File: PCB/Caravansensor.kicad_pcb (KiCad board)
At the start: 2 copper layers, 186 parts, among them J1 Conn_01x06, J5 DB25_Female, Q1 MMBTA92, Q10 BSS138, Q11 BSS138, Q12 BSS138, Q13 BSS83P, Q14 BSS83P, Q15 BSS83P, Q16 BSS83P, Q17 BSS138, Q18 BSS138, Q19 BSS138, Q2 MMBTA92, Q20 BSS138, Q21 BSS138, Q22 BSS138, Q23 BSS138, Q24 BSS138, Q25 BSS83P, Q26 BSS83P, Q27 BSS83P, Q28 BSS83P, Q3 BC856, Q4 BC846, Q5 BSS138, Q6 BSS138, Q7 BSS138, Q8 BSS138, Q9 BSS138, U1 MPX53, U2 MPX53, U3 HX711, U4 HX711, U5 ESP32-WROOM-32D, U6 LMV321, U7 LMV321

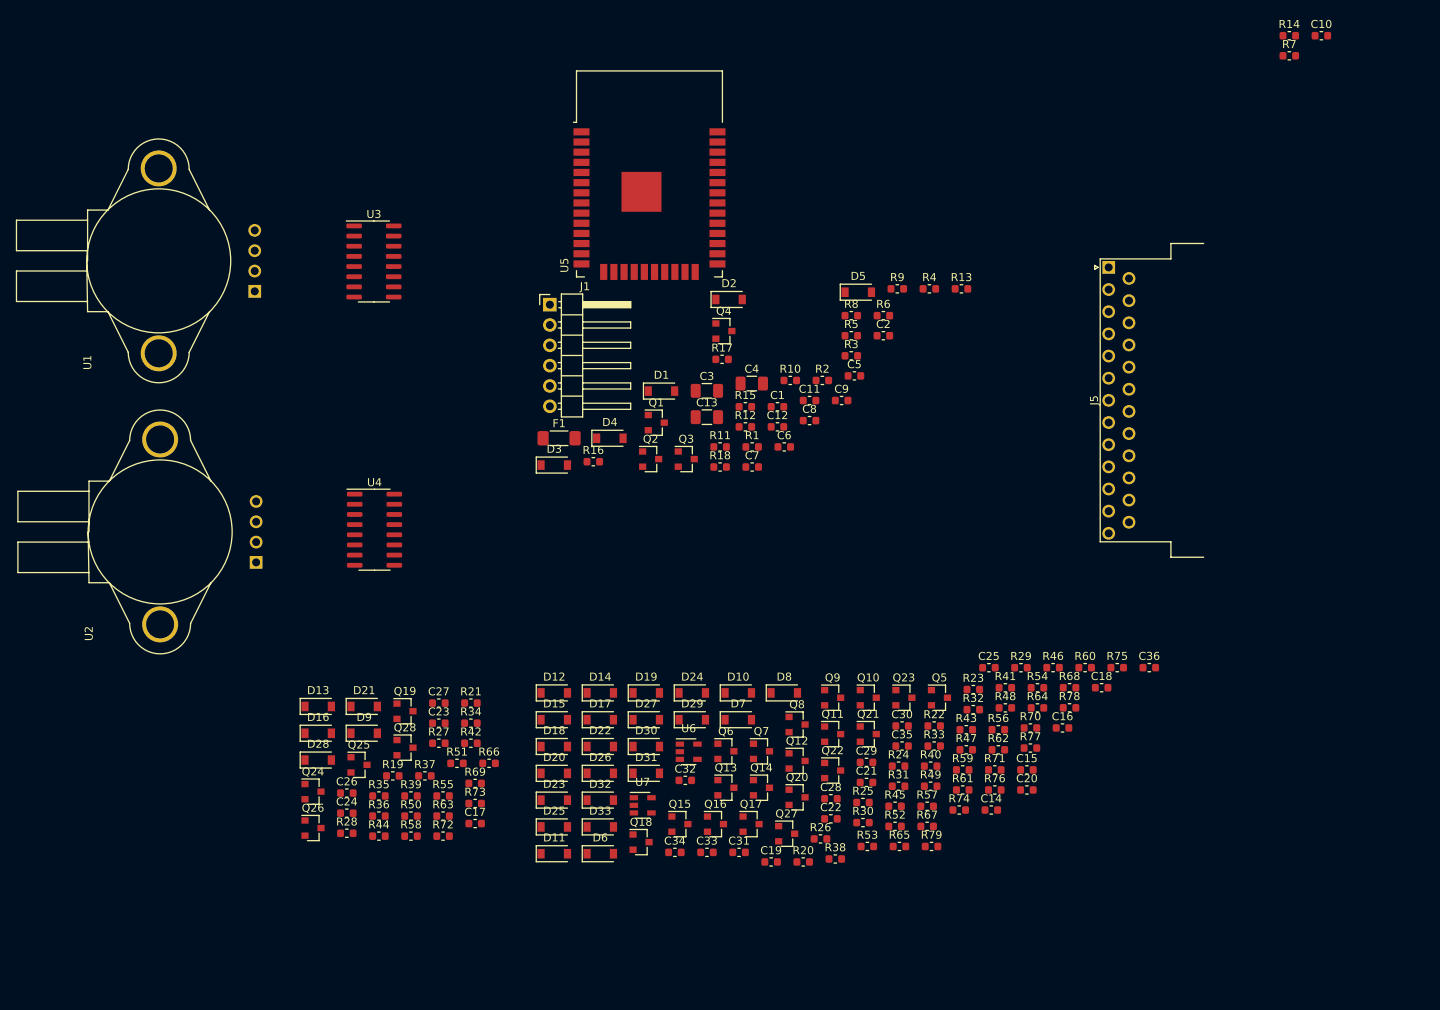
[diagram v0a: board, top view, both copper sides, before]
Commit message: Layout complete, LIN, Added, 1wire added, Power supply added
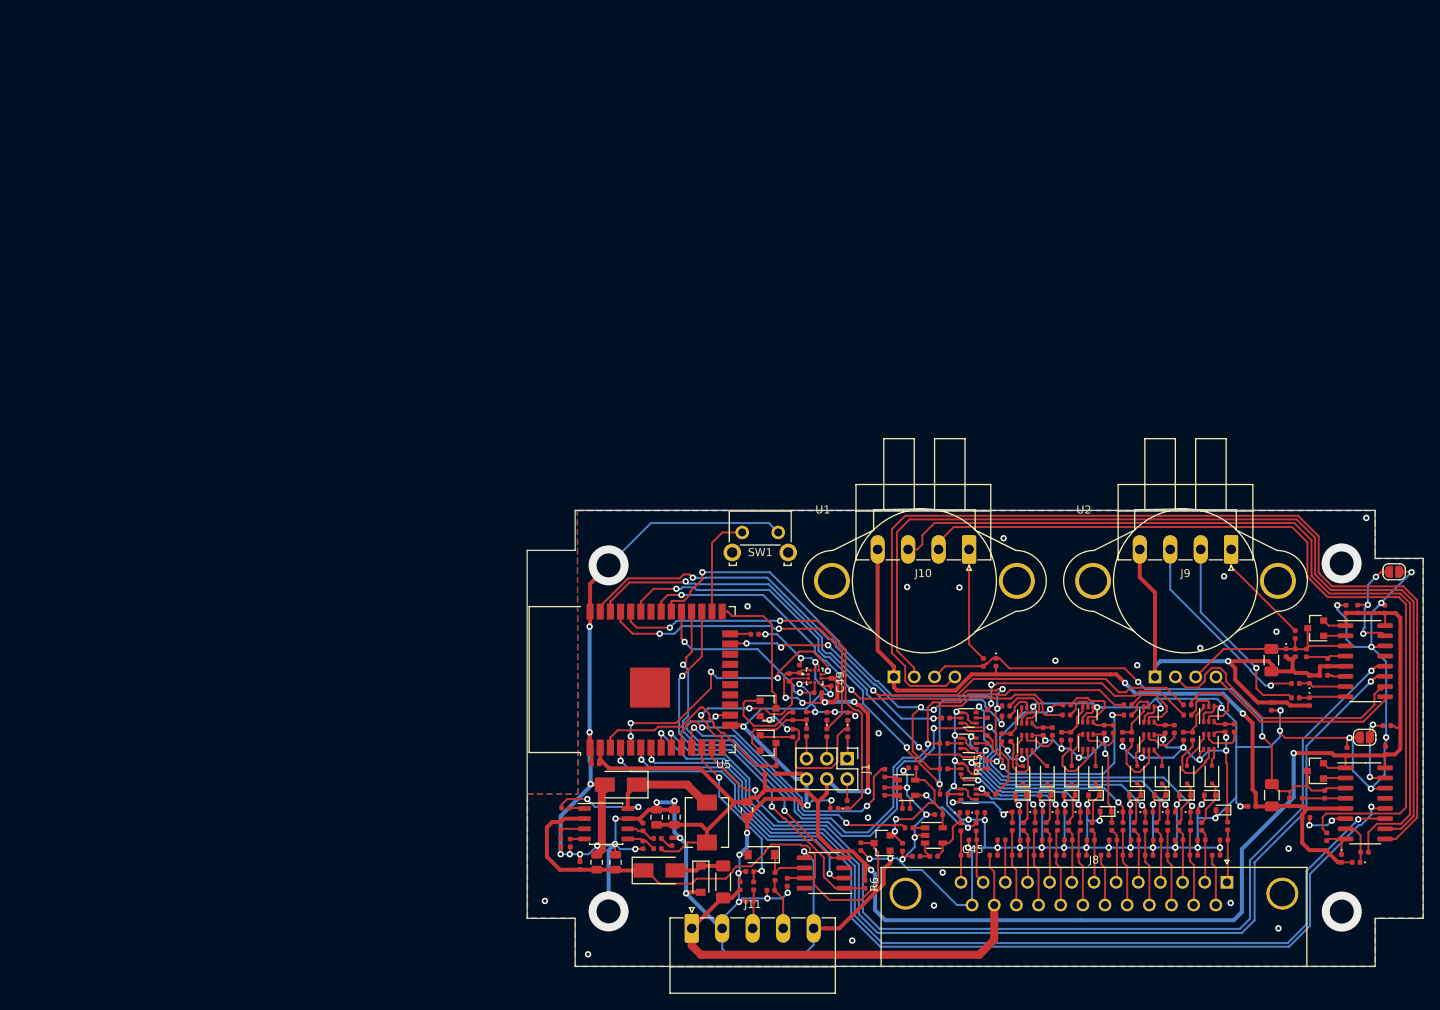
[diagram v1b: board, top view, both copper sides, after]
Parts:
- removed the C27 at (89.9, 123.1)
- removed the C34 at (119.4, 141.8)
- removed the D4 at (111.3, 90.0)
- removed the D5 at (142.4, 71.7)
- removed J5: DB25_Female, Connector_Dsub:DSUB-25_Female_Horizontal_P2.77x2.54mm_EdgePinOffset9.40mm
- removed Q17, Q18, Q19, Q20, Q21, Q22, Q23, Q24: BSS138, Package_TO_SOT_SMD:SOT-23
- removed Q25, Q26, Q27, Q28: BSS83P, Package_TO_SOT_SMD:SOT-23
- removed the R16 at (109.2, 92.9)
- removed the R8 at (141.5, 74.7)
- added C14: 100n, Capacitor_SMD:C_0402_1005Metric, F.Cu at (133.5, 145.5)
- added C15: 100p, Capacitor_SMD:C_0402_1005Metric, F.Cu at (131.4, 146.5)
- added C16: 4u7, Capacitor_SMD:C_0805_2012Metric, F.Cu at (112.0, 143.0)
- added C17: 4u7, Capacitor_SMD:C_0805_2012Metric, F.Cu at (109.7, 143.0)
- added C18: 1n, Capacitor_SMD:C_0402_1005Metric, F.Cu at (117.3, 140.0)
- added C19: 47p, Capacitor_SMD:C_0402_1005Metric, F.Cu at (115.4, 138.6)
- added C20: 100n, Capacitor_SMD:C_0402_1005Metric, F.Cu at (106.4, 140.6)
- added C21: 100n, Capacitor_SMD:C_0402_1005Metric, F.Cu at (105.8, 136.2)
- added C22: 47u, Capacitor_SMD:C_0805_2012Metric, F.Cu at (117.2, 137.4)
- added C23: 47u, Capacitor_SMD:C_0805_2012Metric, F.Cu at (119.4, 137.4)
- added C37: 10n, Capacitor_SMD:C_0402_1005Metric, F.Cu at (165.8, 140.2)
- added C44: 100n, Capacitor_SMD:C_0402_1005Metric, F.Cu at (159.3, 142.1)
- added C47: 100n, Capacitor_SMD:C_0402_1005Metric, F.Cu at (142.7, 141.0)
- added C48: 100n, Capacitor_SMD:C_0402_1005Metric, F.Cu at (147.9, 141.1)
- added C49: 100n, Capacitor_SMD:C_0402_1005Metric, F.Cu at (138.9, 120.5)
- added C50: 47u, Capacitor_SMD:C_0805_2012Metric, F.Cu at (128.5, 136.4)
- added C51: 1n, Capacitor_SMD:C_0402_1005Metric, F.Cu at (132.1, 131.4)
- added C52: 100p, Capacitor_SMD:C_0402_1005Metric, F.Cu at (128.8, 147.8)
- added C53: 100n, Capacitor_SMD:C_0402_1005Metric, F.Cu at (135.0, 118.8)
- added D3: SMF16A, Diode_SMD:D_SOD-123, F.Cu at (130.2, 142.0)
- added D34: RCLAMP0521P-N, Diode_SMD:D_0402_1005Metric, F.Cu at (195.8, 116.8)
- added D35: RCLAMP0521P-N, Diode_SMD:D_0402_1005Metric, F.Cu at (202.8, 142.5)
- added D36: RCLAMP0521P-N, Diode_SMD:D_0402_1005Metric, F.Cu at (198.8, 122.9)
- added D37: RCLAMP0521P-N, Diode_SMD:D_0402_1005Metric, F.Cu at (204.6, 143.0)
- added D38: RCLAMP0521P-N, Diode_SMD:D_0402_1005Metric, F.Cu at (198.8, 120.1)
- added D39: RCLAMP0521P-N, Diode_SMD:D_0402_1005Metric, F.Cu at (128.8, 144.1)
- added D40: RCLAMP0521P-N, Diode_SMD:D_0402_1005Metric, F.Cu at (141.0, 124.8)
- added D41: RCLAMP0521P-N, Diode_SMD:D_0402_1005Metric, F.Cu at (138.4, 124.7)
- added D42: RCLAMP0521P-N, Diode_SMD:D_0402_1005Metric, F.Cu at (135.9, 124.7)
- added D43: RCLAMP0521P-N, Diode_SMD:D_0402_1005Metric, F.Cu at (139.3, 136.3)
- added D6: RCLAMP0521P-N, Diode_SMD:D_0402_1005Metric, F.Cu at (178.7, 136.7)
- added J10: Conn_01x04, Connector_Phoenix_MC:PhoenixContact_MC_1,5_4-G-3.81_1x04_P3.81mm_Horizontal, F.Cu at (156.2, 103.9)
- added J11: Conn_01x05, Connector_Phoenix_MC:PhoenixContact_MC_1,5_5-G-3.81_1x05_P3.81mm_Horizontal, F.Cu at (121.5, 151.3)
- added J8: DB25_Female, Connector_Dsub:DSUB-25_Female_Horizontal_P2.77x2.84mm_EdgePinOffset7.70mm_Housed_MountingHolesOffset9.12mm, F.Cu at (188.4, 145.5)
- added J9: Conn_01x04, Connector_Phoenix_MC:PhoenixContact_MC_1,5_4-G-3.81_1x04_P3.81mm_Horizontal, F.Cu at (189.0, 103.9)
- added JP2: Jumper_2_Open, Jumper:SolderJumper-2_P1.3mm_Open_RoundedPad1.0x1.5mm, F.Cu at (205.7, 127.4)
- added JP3: Jumper_2_Open, Jumper:SolderJumper-2_P1.3mm_Open_RoundedPad1.0x1.5mm, F.Cu at (209.3, 106.7)
- added L1: SLO0630H6R8MTT, Inductor_SMD:L_Neosid_SM-PIC0512H, F.Cu at (123.4, 138.0)
- added L2: L, Inductor_SMD:L_0402_1005Metric, F.Cu at (191.6, 136.0)
- added L3: L, Inductor_SMD:L_0402_1005Metric, F.Cu at (194.0, 123.5)
- added R12: 29k4, Resistor_SMD:R_0402_1005Metric, F.Cu at (119.1, 140.4)
- added R7: 100r, Resistor_SMD:R_0402_1005Metric, F.Cu at (132.0, 144.8)
- added R80: 100r, Resistor_SMD:R_0402_1005Metric, F.Cu at (158.0, 118.0)
- added R81: 100r, Resistor_SMD:R_0402_1005Metric, F.Cu at (200.9, 139.8)
- added R82: 100r, Resistor_SMD:R_0402_1005Metric, F.Cu at (205.6, 141.7)
- added R83: 100r, Resistor_SMD:R_0402_1005Metric, F.Cu at (197.0, 114.5)
- added R84: 100r, Resistor_SMD:R_0402_1005Metric, F.Cu at (197.0, 122.4)
- added R85: 100r, Resistor_SMD:R_0402_1005Metric, F.Cu at (197.0, 120.7)
- added R86: 4k7, Resistor_SMD:R_0402_1005Metric, F.Cu at (133.7, 119.9)
- added R87: 4k7, Resistor_SMD:R_0402_1005Metric, F.Cu at (137.3, 121.8)
- added R88: 12k, Resistor_SMD:R_0402_1005Metric, F.Cu at (130.7, 131.4)
- added R89: 100r, Resistor_SMD:R_0402_1005Metric, F.Cu at (129.3, 145.9)
- added R90: 10k, Resistor_SMD:R_0402_1005Metric, F.Cu at (208.4, 125.9)
- added R91: 10k, Resistor_SMD:R_0402_1005Metric, F.Cu at (204.8, 111.3)
- added SW1: TS-1093A-A12B3-D2, Button_Switch_THT:SW_Tactile_SKHH_Angled, F.Cu at (127.9, 101.8)
- added U10: BMP388, Caravansensor:PQFN50P200X200X80-10N, F.Cu at (136.9, 119.8)
- added U11: ME6209A50M3G, Package_TO_SOT_SMD:SOT-23, F.Cu at (145.3, 140.6)
- added U6: TJA1021T, Package_SO:SOIC-8_3.9x4.9mm_P1.27mm, F.Cu at (138.1, 144.3)
- added U7: TPS54331D, Package_SO:SOIC-8_3.9x4.9mm_P1.27mm, F.Cu at (110.8, 138.2)
- C1, C10, C11, C12, C2, C5, C6, C7, C8, C9: footprint Capacitor_SMD:C_0603_1608Metric -> Capacitor_SMD:C_0402_1005Metric
- C13: value 10u -> 100n; footprint Capacitor_SMD:C_1206_3216Metric -> Capacitor_SMD:C_0402_1005Metric
- C24: renamed from C14; footprint Capacitor_SMD:C_0603_1608Metric -> Capacitor_SMD:C_0402_1005Metric
- C25: renamed from C15; footprint Capacitor_SMD:C_0603_1608Metric -> Capacitor_SMD:C_0402_1005Metric
- C26: renamed from C16; footprint Capacitor_SMD:C_0603_1608Metric -> Capacitor_SMD:C_0402_1005Metric
- C27: renamed from C17; footprint Capacitor_SMD:C_0603_1608Metric -> Capacitor_SMD:C_0402_1005Metric
- C28: renamed from C18; footprint Capacitor_SMD:C_0603_1608Metric -> Capacitor_SMD:C_0402_1005Metric
- C29: renamed from C19; footprint Capacitor_SMD:C_0603_1608Metric -> Capacitor_SMD:C_0402_1005Metric
- C30: renamed from C20; footprint Capacitor_SMD:C_0603_1608Metric -> Capacitor_SMD:C_0402_1005Metric
- C31: renamed from C21; footprint Capacitor_SMD:C_0603_1608Metric -> Capacitor_SMD:C_0402_1005Metric
- C32: renamed from C22; footprint Capacitor_SMD:C_0603_1608Metric -> Capacitor_SMD:C_0402_1005Metric
- C33: renamed from C23; footprint Capacitor_SMD:C_0603_1608Metric -> Capacitor_SMD:C_0402_1005Metric
- C34: renamed from C24; footprint Capacitor_SMD:C_0603_1608Metric -> Capacitor_SMD:C_0402_1005Metric
- C35: renamed from C25; footprint Capacitor_SMD:C_0603_1608Metric -> Capacitor_SMD:C_0402_1005Metric
- C36: renamed from C26; footprint Capacitor_SMD:C_0603_1608Metric -> Capacitor_SMD:C_0402_1005Metric
- C38: renamed from C28; footprint Capacitor_SMD:C_0603_1608Metric -> Capacitor_SMD:C_0402_1005Metric
- C39: renamed from C29; footprint Capacitor_SMD:C_0603_1608Metric -> Capacitor_SMD:C_0402_1005Metric
- C40: renamed from C30; footprint Capacitor_SMD:C_0603_1608Metric -> Capacitor_SMD:C_0402_1005Metric
- C41: renamed from C31; footprint Capacitor_SMD:C_0603_1608Metric -> Capacitor_SMD:C_0402_1005Metric
- C42: renamed from C32; footprint Capacitor_SMD:C_0603_1608Metric -> Capacitor_SMD:C_0402_1005Metric
- C43: renamed from C33; footprint Capacitor_SMD:C_0603_1608Metric -> Capacitor_SMD:C_0402_1005Metric
- C45: renamed from C35; footprint Capacitor_SMD:C_0603_1608Metric -> Capacitor_SMD:C_0402_1005Metric
- C46: renamed from C36; footprint Capacitor_SMD:C_0603_1608Metric -> Capacitor_SMD:C_0402_1005Metric
- D10, D11, D12, D22, D23, D24: value D -> 1N4148WS; footprint Diode_SMD:D_SOD-123 -> Diode_SMD:D_SOD-323F
- D13, D25: value D -> ESD5Z15V; footprint Diode_SMD:D_SOD-123 -> Diode_SMD:D_SOD-523
- D14, D15, D16, D26, D27, D28, D29, D30: value SMF16A -> ESD5Z15V; footprint Diode_SMD:D_SOD-123 -> Diode_SMD:D_SOD-523
- D17, D18, D19, D20, D31, D32, D33, D7, D8: value SMF16A -> RCLAMP0521P-N; footprint Diode_SMD:D_SOD-123 -> Diode_SMD:D_0402_1005Metric
- D2: value D -> B340A; footprint Diode_SMD:D_SOD-123 -> Diode_SMD:D_SMA
- D21, D9: value SMF16A -> 1N4148WS; footprint Diode_SMD:D_SOD-123 -> Diode_SMD:D_SOD-323F
- D4: renamed from D3; value D -> B340A; footprint Diode_SMD:D_SOD-123 -> Diode_SMD:D_SMA
- D5: renamed from D6; value SMF16A -> RCLAMP0521P-N; footprint Diode_SMD:D_SOD-123 -> Diode_SMD:D_0402_1005Metric
- J1: value Conn_01x06 -> Conn_02x03_Odd_Even; footprint Connector_PinHeader_2.54mm:PinHeader_1x06_P2.54mm_Horizontal -> Connector_PinHeader_2.54mm:PinHeader_2x03_P2.54mm_Vertical
- Q1, Q2: value MMBTA92 -> MMBTA92-Transistor_BJT
- Q10, Q9: value BSS138 -> LBSS84DW; footprint Package_TO_SOT_SMD:SOT-23 -> Package_TO_SOT_SMD:SOT-363_SC-70-6
- Q11, Q12, Q5, Q6, Q7, Q8: value BSS138 -> LBSS260DW; footprint Package_TO_SOT_SMD:SOT-23 -> Package_TO_SOT_SMD:SOT-363_SC-70-6
- Q13, Q14: value BSS83P -> LBSS260DW; footprint Package_TO_SOT_SMD:SOT-23 -> Package_TO_SOT_SMD:SOT-363_SC-70-6
- Q15, Q16: value BSS83P -> LBSS84DW; footprint Package_TO_SOT_SMD:SOT-23 -> Package_TO_SOT_SMD:SOT-363_SC-70-6
- Q3: value BC856 -> MMBT5401
- Q4: value BC846 -> MMBT5401
- R1, R19, R2, R20, R21, R22, R23, R24, R25, R26, R27, R28, R29, R3, R30, R31, R32, R33, R34, R35, R36, R37, R38, R39, R4, R40, R41, R42, R43, R44, R45, R46, R47, R48, R49, R5, R50, R51, R52, R53, R54, R55, R56, R57, R58, R59, R60, R61, R62, R63, R64, R65, R66, R71, R72, R75, R76, R77, R78, R79: footprint Resistor_SMD:R_0603_1608Metric -> Resistor_SMD:R_0402_1005Metric
- R10: value 10k -> 332k; footprint Resistor_SMD:R_0603_1608Metric -> Resistor_SMD:R_0402_1005Metric
- R11: value 10k -> 68k1; footprint Resistor_SMD:R_0603_1608Metric -> Resistor_SMD:R_0402_1005Metric
- R13: renamed from R12; value 10k -> 100r; footprint Resistor_SMD:R_0603_1608Metric -> Resistor_SMD:R_0402_1005Metric
- R14, R15: value 10k -> 100r; footprint Resistor_SMD:R_0603_1608Metric -> Resistor_SMD:R_0402_1005Metric
- R16: renamed from R13; value 1k -> 100r; footprint Resistor_SMD:R_0603_1608Metric -> Resistor_SMD:R_0402_1005Metric
- R17: value 10k -> 10k2; footprint Resistor_SMD:R_0603_1608Metric -> Resistor_SMD:R_0402_1005Metric
- R18: value 10k -> 3k24; footprint Resistor_SMD:R_0603_1608Metric -> Resistor_SMD:R_0402_1005Metric
- R6: renamed from R9; footprint Resistor_SMD:R_0603_1608Metric -> Resistor_SMD:R_0402_1005Metric
- R67, R69: value R -> 1k; footprint Resistor_SMD:R_0603_1608Metric -> Resistor_SMD:R_0402_1005Metric
- R68, R70: value R -> 200k; footprint Resistor_SMD:R_0603_1608Metric -> Resistor_SMD:R_0402_1005Metric
- R73, R74: value R -> 100k; footprint Resistor_SMD:R_0603_1608Metric -> Resistor_SMD:R_0402_1005Metric
- R8: renamed from R7; value 1k -> 10k; footprint Resistor_SMD:R_0603_1608Metric -> Resistor_SMD:R_0402_1005Metric
- R9: renamed from R6; footprint Resistor_SMD:R_0603_1608Metric -> Resistor_SMD:R_0402_1005Metric
- moved U3 141.2 mm to (205.7, 135.6)
- moved U2 128.3 mm to (183.3, 107.8), turned to 0 degrees
- moved U4 124.9 mm to (205.7, 117.9)
- moved D16 111.7 mm to (186.3, 134.6), turned to 180 degrees
- moved R14 104.6 mm to (138.4, 126.8), turned to 90 degrees
- moved U1 103.7 mm to (150.6, 107.8), turned to 0 degrees
- moved R8 103.3 mm to (134.2, 124.7), turned to 90 degrees
- moved R28 103.1 mm to (180.7, 126.3), turned to 90 degrees
- moved D13 102.7 mm to (177.0, 134.6), turned to 180 degrees
- moved D28 97.1 mm to (171.8, 134.6), turned to 180 degrees
- moved D9 96.8 mm to (177.2, 132.0), turned to 90 degrees
- moved R36 95.8 mm to (178.2, 138.5), turned to 270 degrees
- moved R34 95.4 mm to (189.4, 126.2), turned to 90 degrees
- moved Q1 93.2 mm to (199.5, 131.6), turned to 180 degrees
- moved R35 93.1 mm to (175.5, 138.5), turned to 270 degrees
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- renumbered U6 to U8, U7 to U9
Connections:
- C1 pad 2: GND -> Net-(C1-Pad2)
- C2 pad 2: GND -> Net-(C2-Pad2)
- C3 pad 2: GND -> Net-(C1-Pad2)
- C4 pad 2: GND -> Net-(C2-Pad2)
- C5 pad 2: GND -> Net-(C1-Pad2)
- C6 pad 2: GND -> Net-(C2-Pad2)
- D13 pad 2: Net-(D13-Pad2) -> GND
- D17 pad 1: Net-(D13-Pad1) -> Net-(D17-Pad1)
- D21 pad 2: GND -> Net-(D21-Pad2)
- D25 pad 1: Net-(D25-Pad1) -> Net-(D21-Pad1)
- D25 pad 2: Net-(D25-Pad2) -> GND
- D29 pad 1: Net-(D25-Pad1) -> VCC
- D30 pad 1: VCC -> VCCQ
- D31 pad 1: VCCQ -> Net-(D31-Pad1)
- D33 pad 1: Net-(D33-Pad1) -> Net-(C1-Pad1)
- D33 pad 2: GND -> Net-(C1-Pad2)
- D4 pad 2: Net-(D3-Pad2) -> GND
- D5 pad 1: Net-(D6-Pad1) -> Net-(D5-Pad1)
- D9 pad 1: Net-(D9-Pad1) -> Net-(D13-Pad1)
- D9 pad 2: GND -> Net-(D9-Pad2)
- J1 pad 4: Net-(J1-Pad4) -> +3V3
- J1 pad 6: Net-(J1-Pad6) -> GND
- Q10 pad 1: Net-(Q10-Pad1) -> VCC
- Q10 pad 2: GND -> Net-(Q10-Pad2)
- Q10 pad 3: Net-(D7-Pad1) -> Net-(D12-Pad2)
- Q11 pad 1: Net-(Q11-Pad1) -> GND
- Q11 pad 2: GND -> Net-(Q11-Pad2)
- Q11 pad 3: Net-(D8-Pad1) -> Net-(D18-Pad1)
- Q12 pad 1: Net-(Q12-Pad1) -> GND
- Q12 pad 2: GND -> Net-(Q12-Pad2)
- Q12 pad 3: Net-(D9-Pad1) -> Net-(D20-Pad1)
- Q13 pad 1: Net-(Q13-Pad1) -> GND
- Q13 pad 2: VCC -> Net-(Q13-Pad2)
- Q13 pad 3: Net-(D10-Pad2) -> Net-(Q13-Pad3)
- Q14 pad 1: Net-(Q14-Pad1) -> GND
- Q14 pad 2: VCC -> Net-(Q14-Pad2)
- Q14 pad 3: Net-(D11-Pad2) -> Net-(Q14-Pad3)
- Q15 pad 1: Net-(Q15-Pad1) -> VCCQ
- Q15 pad 2: VCC -> Net-(Q15-Pad2)
- Q15 pad 3: Net-(D12-Pad2) -> Net-(D22-Pad2)
- Q16 pad 1: Net-(Q16-Pad1) -> VCCQ
- Q16 pad 2: VCC -> Net-(Q16-Pad2)
- Q16 pad 3: Net-(D13-Pad2) -> Net-(D24-Pad2)
- Q3 pad 2: Net-(Q3-Pad2) -> PGM_DTR
- Q3 pad 3: Net-(Q3-Pad3) -> GPIO_0
- Q4 pad 2: Net-(Q4-Pad2) -> PGM_CTS
- Q4 pad 3: Net-(Q4-Pad3) -> Reset
- Q5 pad 1: Net-(Q5-Pad1) -> GND
- Q5 pad 2: GND -> Net-(Q5-Pad2)
- Q6 pad 1: Net-(Q6-Pad1) -> GND
- Q6 pad 2: GND -> Net-(Q6-Pad2)
- Q7 pad 1: Net-(Q7-Pad1) -> GND
- Q7 pad 2: GND -> Net-(Q7-Pad2)
- Q7 pad 3: Net-(Q7-Pad3) -> Net-(D6-Pad1)
- Q8 pad 1: Net-(Q8-Pad1) -> GND
- Q8 pad 2: GND -> Net-(Q8-Pad2)
- Q8 pad 3: Net-(Q8-Pad3) -> Net-(D8-Pad1)
- Q9 pad 1: Net-(Q9-Pad1) -> VCC
- Q9 pad 2: GND -> Net-(Q9-Pad2)
- Q9 pad 3: Net-(D6-Pad1) -> Net-(D10-Pad2)
- R10 pad 1: Net-(R10-Pad1) -> +BATT
- R11 pad 1: Net-(R11-Pad1) -> Net-(R10-Pad2)
- R11 pad 2: Net-(R11-Pad2) -> GND
- R13 pad 2: Net-(R12-Pad2) -> PGM_DTR
- R14 pad 2: Net-(R14-Pad2) -> PGM_TX
- R15 pad 2: Net-(R15-Pad2) -> PGM_CTS
- R16 pad 1: Net-(R13-Pad1) -> PGM_RX
- R17 pad 1: Net-(R17-Pad1) -> +3V3
- R18 pad 1: Net-(R18-Pad1) -> Net-(R17-Pad2)
- R18 pad 2: Net-(R18-Pad2) -> GND
- R19 pad 1: Net-(Q5-Pad1) -> Net-(Q5-Pad2)
- R2 pad 2: GND -> Net-(C1-Pad2)
- R20 pad 1: Net-(Q6-Pad1) -> Net-(Q5-Pad5)
- R21 pad 1: Net-(Q7-Pad1) -> Net-(Q6-Pad2)
- R22 pad 1: Net-(Q8-Pad1) -> Net-(Q6-Pad5)
- R23 pad 1: Net-(Q9-Pad1) -> Net-(Q7-Pad2)
- R24 pad 1: Net-(Q10-Pad1) -> Net-(Q7-Pad5)
- R25 pad 1: Net-(Q11-Pad1) -> Net-(Q8-Pad2)
- R26 pad 1: Net-(Q12-Pad1) -> Net-(Q8-Pad5)
- R27 pad 2: Net-(Q5-Pad3) -> Net-(Q5-Pad6)
- R28 pad 2: Net-(Q6-Pad3) -> Net-(Q5-Pad3)
- R29 pad 2: Net-(Q7-Pad3) -> Net-(Q6-Pad6)
- R30 pad 2: Net-(Q8-Pad3) -> Net-(Q6-Pad3)
- R31 pad 1: Net-(Q13-Pad1) -> Net-(Q9-Pad2)
- R31 pad 2: Net-(Q5-Pad3) -> Net-(Q5-Pad6)
- R32 pad 1: Net-(Q14-Pad1) -> Net-(Q9-Pad5)
- R32 pad 2: Net-(Q6-Pad3) -> Net-(Q5-Pad3)
- R33 pad 1: Net-(Q15-Pad1) -> Net-(Q10-Pad2)
- R33 pad 2: Net-(Q7-Pad3) -> Net-(Q6-Pad6)
- R34 pad 1: Net-(Q16-Pad1) -> Net-(Q10-Pad5)
- R34 pad 2: Net-(Q8-Pad3) -> Net-(Q6-Pad3)
- R35 pad 1: Net-(D6-Pad1) -> Net-(D5-Pad1)
- R36 pad 1: Net-(D7-Pad1) -> Net-(D6-Pad1)
- R37 pad 1: Net-(D8-Pad1) -> Net-(D7-Pad1)
- R38 pad 1: Net-(D9-Pad1) -> Net-(D8-Pad1)
- R39 pad 1: Net-(D10-Pad1) -> Net-(D13-Pad1)
- R4 pad 2: GND -> Net-(C2-Pad2)
- R40 pad 1: Net-(D11-Pad1) -> Net-(D10-Pad1)
- R41 pad 1: Net-(D12-Pad1) -> Net-(D11-Pad1)
- R42 pad 1: Net-(D13-Pad1) -> Net-(D12-Pad1)
- R43 pad 1: Net-(Q17-Pad1) -> Net-(Q11-Pad2)
- R44 pad 1: Net-(Q18-Pad1) -> Net-(Q11-Pad5)
- R45 pad 1: Net-(Q19-Pad1) -> Net-(Q12-Pad2)
- R46 pad 1: Net-(Q20-Pad1) -> Net-(Q12-Pad5)
- R47 pad 1: Net-(Q21-Pad1) -> Net-(Q13-Pad2)
- R48 pad 1: Net-(Q22-Pad1) -> Net-(Q13-Pad5)
- R49 pad 1: Net-(Q23-Pad1) -> Net-(Q14-Pad2)
- R50 pad 1: Net-(Q24-Pad1) -> Net-(Q14-Pad5)
- R51 pad 2: Net-(Q21-Pad3) -> Net-(Q13-Pad6)
- R52 pad 2: Net-(Q22-Pad3) -> Net-(Q13-Pad3)
- R53 pad 2: Net-(Q23-Pad3) -> Net-(Q14-Pad6)
- R54 pad 2: Net-(Q24-Pad3) -> Net-(Q14-Pad3)
- R55 pad 1: Net-(Q25-Pad1) -> Net-(Q15-Pad2)
- R55 pad 2: Net-(Q21-Pad3) -> Net-(Q13-Pad6)
- R56 pad 1: Net-(Q26-Pad1) -> Net-(Q15-Pad5)
- R56 pad 2: Net-(Q22-Pad3) -> Net-(Q13-Pad3)
- R57 pad 1: Net-(Q27-Pad1) -> Net-(Q16-Pad2)
- R57 pad 2: Net-(Q23-Pad3) -> Net-(Q14-Pad6)
- R58 pad 1: Net-(Q28-Pad1) -> Net-(Q16-Pad5)
- R58 pad 2: Net-(Q24-Pad3) -> Net-(Q14-Pad3)
- R59 pad 1: Net-(D18-Pad1) -> Net-(D17-Pad1)
- R6 pad 1: Net-(R9-Pad1) -> +3V3
- R6 pad 2: Net-(R9-Pad2) -> LIN_RX
- R60 pad 1: Net-(D19-Pad1) -> Net-(D18-Pad1)
- R61 pad 1: Net-(D20-Pad1) -> Net-(D19-Pad1)
- R62 pad 1: Net-(D21-Pad1) -> Net-(D20-Pad1)
- R63 pad 1: Net-(D22-Pad1) -> Net-(D21-Pad1)
- R64 pad 1: Net-(D23-Pad1) -> Net-(D22-Pad1)
- R65 pad 1: Net-(D24-Pad1) -> Net-(D23-Pad1)
- R66 pad 1: Net-(D25-Pad1) -> Net-(D24-Pad1)
- R73 pad 1: Net-(D32-Pad1) -> Net-(D31-Pad1)
- R74 pad 1: Net-(D33-Pad1) -> Net-(D32-Pad1)
- R75 pad 2: Net-(D32-Pad1) -> Net-(D31-Pad1)
- R76 pad 2: Net-(D33-Pad1) -> Net-(D32-Pad1)
- R8 pad 1: Net-(R7-Pad1) -> PGM_CTS
- R8 pad 2: Net-(R7-Pad2) -> Net-(Q3-Pad1)
- R9 pad 1: Net-(R6-Pad1) -> Net-(Q4-Pad1)
- R9 pad 2: Net-(R6-Pad2) -> PGM_DTR
- U1 pad 1: GND -> Net-(C1-Pad2)
- U2 pad 1: GND -> Net-(C2-Pad2)
- U3 pad 5: GND -> Net-(C1-Pad2)
- U3 pad 7: Net-(U3-Pad7) -> INA_N_2
- U3 pad 8: Net-(U3-Pad8) -> INA_P_2
- U4 pad 5: GND -> Net-(C2-Pad2)
- U4 pad 7: Net-(U4-Pad7) -> INA_N_1
- U4 pad 8: Net-(U4-Pad8) -> INA_P_1
- U5 pad 12: Net-(U5-Pad12) -> 1_Wire
- U5 pad 13: Net-(U5-Pad13) -> FW_75
- U5 pad 14: Net-(U5-Pad14) -> SCL
- U5 pad 16: Net-(U5-Pad16) -> FW_100
- U5 pad 23: 1_Wire -> FW_50
- U5 pad 25: Net-(U5-Pad25) -> GPIO_0
- U5 pad 26: Net-(U5-Pad26) -> WLAN
- U5 pad 29: Net-(U5-Pad29) -> SDA
- U5 pad 3: Net-(U5-Pad3) -> Reset
- U5 pad 30: Net-(U5-Pad30) -> FW_25
- U5 pad 31: Net-(U5-Pad31) -> WW_100
- U5 pad 33: Net-(U5-Pad33) -> WW_75
- U5 pad 34: Net-(U5-Pad34) -> PGM_RX
- U5 pad 35: Net-(U5-Pad35) -> PGM_TX
- U5 pad 36: Net-(U5-Pad36) -> WW_50
- U5 pad 37: Net-(U5-Pad37) -> WW_25
- U5 pad 39: GND -> (no net)
- U5 pad 4: Net-(U5-Pad4) -> LIN_SLP
- U5 pad 5: Net-(U5-Pad5) -> BME_INT
- U8 pad 4: Net-(D32-Pad1) -> Net-(D31-Pad1)
- U9 pad 4: Net-(D33-Pad1) -> Net-(D32-Pad1)
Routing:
- net GND: track 0.00 -> 632.0 mm, vias 0 -> 85
- net +3V3: track 0.00 -> 240.3 mm, vias 0 -> 7
- net Net-(U1-Pad4): track 0.00 -> 132.3 mm
- net Net-(U4-Pad11): track 0.00 -> 130.2 mm, vias 0 -> 2
- net Net-(U4-Pad12): track 0.00 -> 129.4 mm, vias 0 -> 2
- net Net-(U1-Pad2): track 0.00 -> 122.2 mm
- net Net-(U3-Pad12): track 0.00 -> 121.2 mm, vias 0 -> 2
- net Net-(U3-Pad11): track 0.00 -> 118.3 mm, vias 0 -> 2
- net Net-(J10-Pad3): track 0.00 -> 106.6 mm
- net Net-(J10-Pad2): track 0.00 -> 105.1 mm
- net Net-(C1-Pad2): track 0.00 -> 101.2 mm, vias 0 -> 2
- net FW_100: track 0.00 -> 82.9 mm, vias 0 -> 2
- net FW_25: track 0.00 -> 80.4 mm, vias 0 -> 3
- net WW_25: track 0.00 -> 80.3 mm, vias 0 -> 3
- net FW_75: track 0.00 -> 77.9 mm, vias 0 -> 4
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- added copper zone on B.Cu, net GND
- added copper zone on F.Cu, net GND
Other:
- board outline added: 112 x 57 mm
- net class Medium added: clearance 0.2, trace_width 0.3, via_dia 0.8, via_drill 0.4
- net class Octo added: clearance 0.2, trace_width 0.25, via_dia 1, via_drill 0.5
- net class Power added: clearance 0.2, trace_width 1, via_dia 1, via_drill 0.5
- net class Power_high added: clearance 0.2, trace_width 1.5, via_dia 0.8, via_drill 0.4
- net class Power_smal added: clearance 0.2, trace_width 0.5, via_dia 0.8, via_drill 0.4
- rule pad_to_mask_clearance: 0.051 -> 0
